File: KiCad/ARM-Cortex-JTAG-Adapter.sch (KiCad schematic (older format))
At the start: 4 parts, among them J1 Breakout I/O, J2 Power

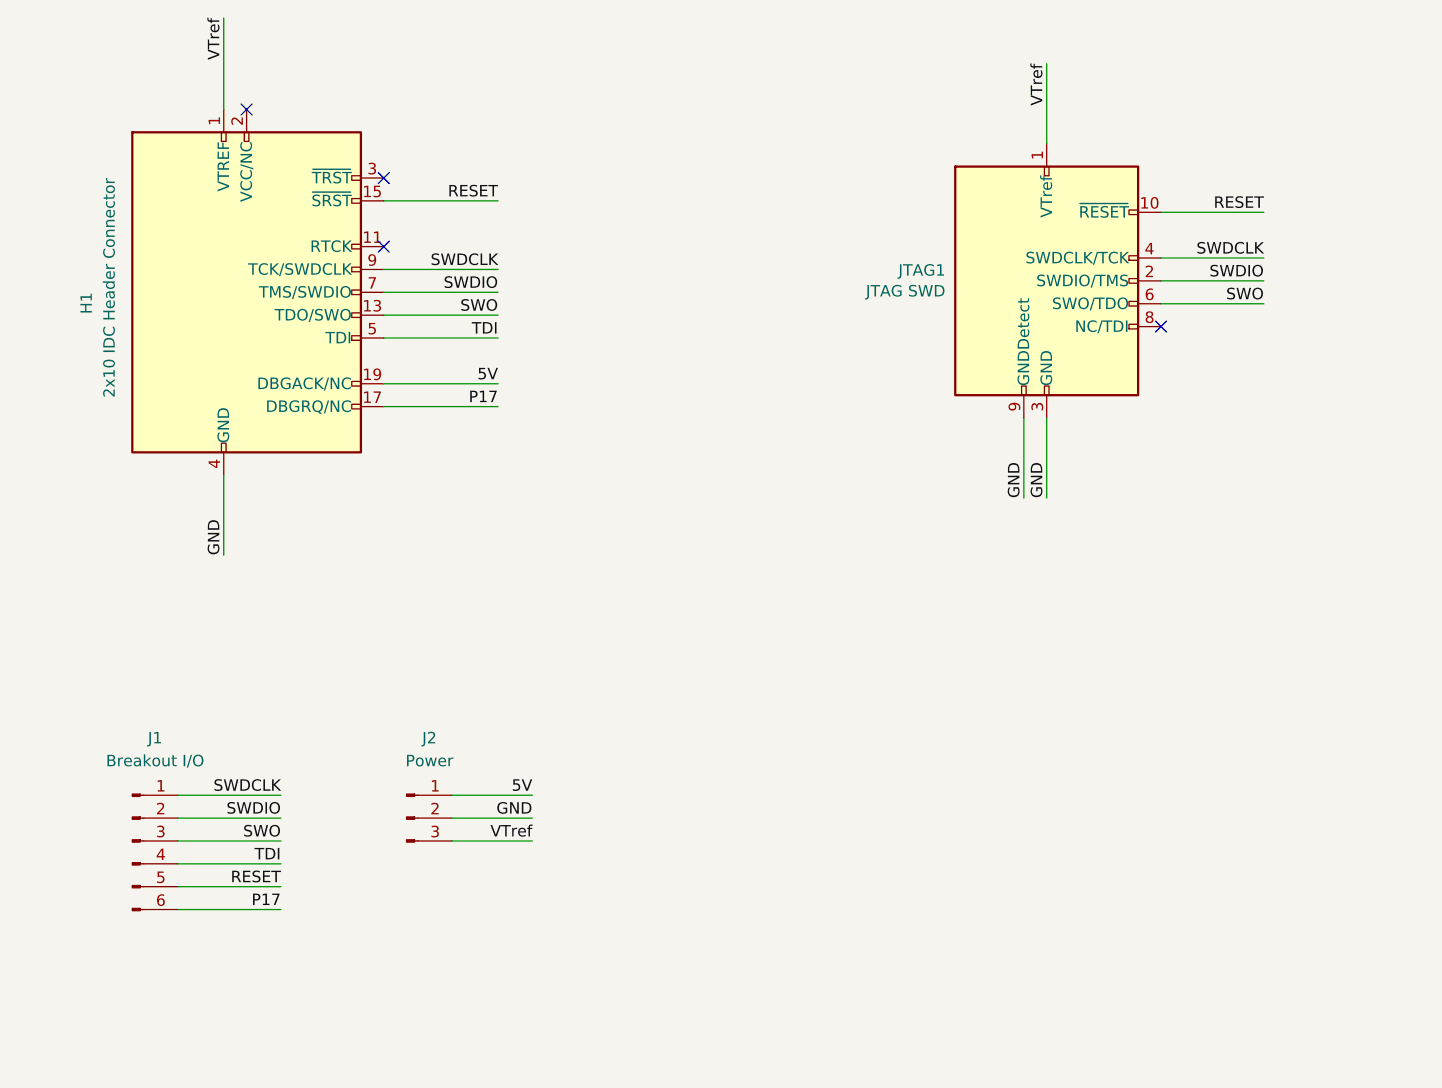
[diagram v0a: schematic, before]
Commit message: Updating schematic and PCB layout.
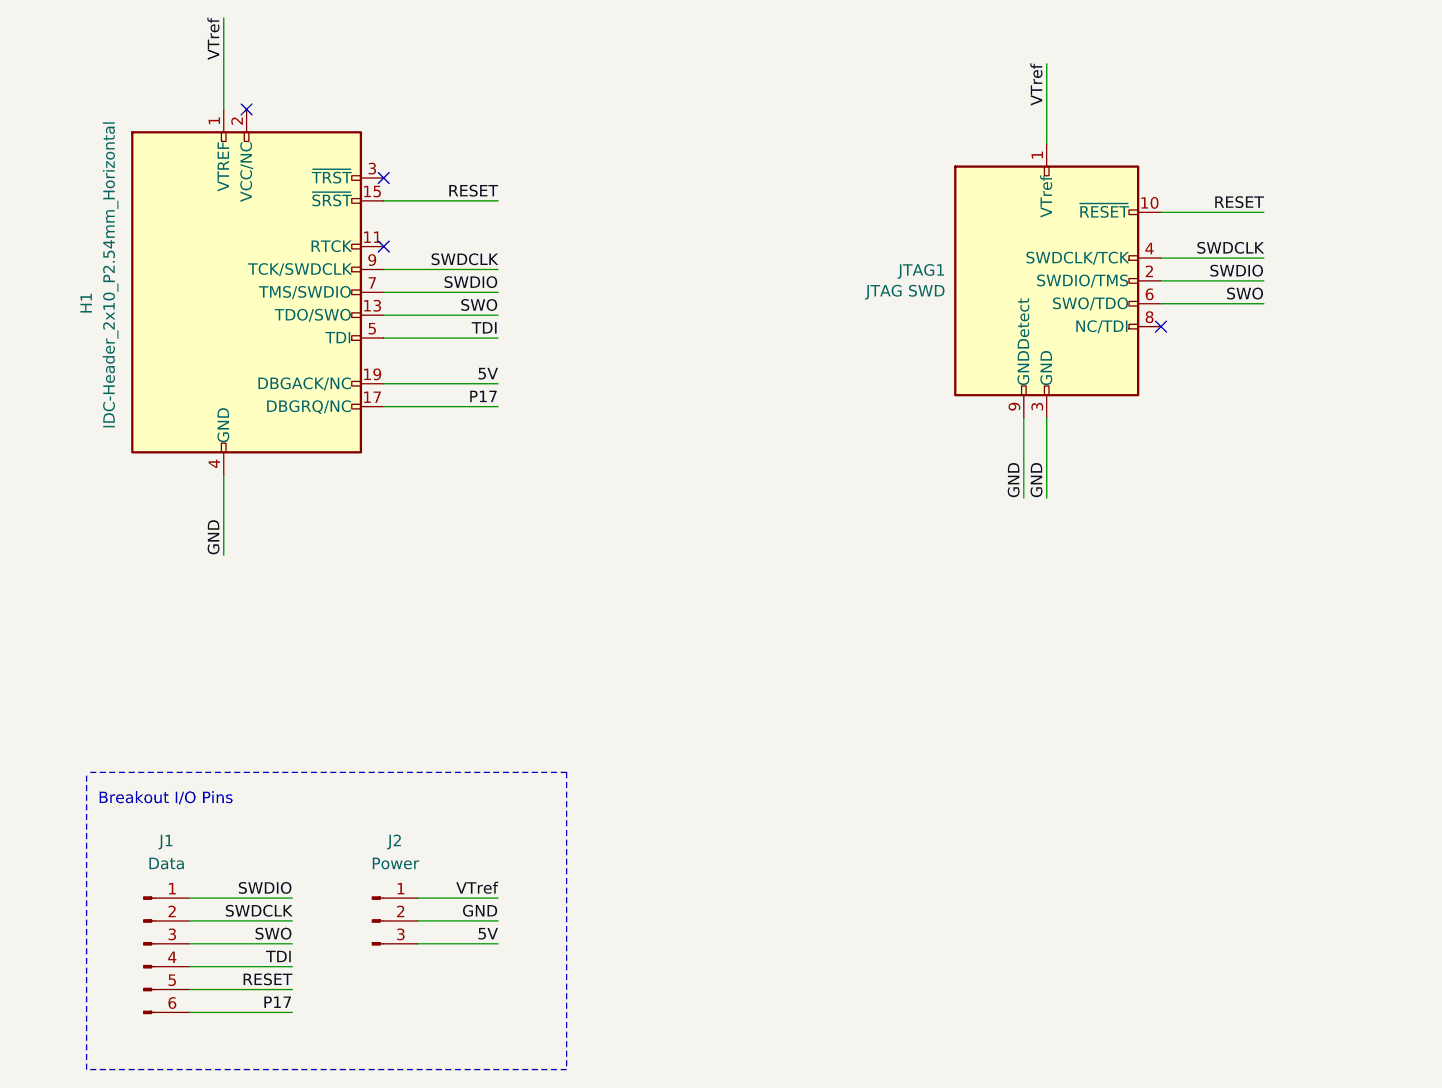
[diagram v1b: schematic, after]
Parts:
- H1: value 2x10 IDC Header Connector -> IDC-Header_2x10_P2.54mm_Horizontal
- J1: value Breakout I/O -> Data
- JTAG1: footprint Connector_PinHeader_1.27mm:PinHeader_2x05_P1.27mm_Vertical_SMD -> Connector_PinHeader_1.27mm:PinHeader_2x05_P1.27mm_Vertical
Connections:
- net 5V: now also J2.3 (Pin_3); no longer J2.1 (Pin_1)
- net SWDCLK: now also J1.2 (Pin_2); no longer J1.1 (Pin_1)
- net SWDIO: now also J1.1 (Pin_1); no longer J1.2 (Pin_2)
- net VTref: now also J2.1 (Pin_1); no longer J2.3 (Pin_3)
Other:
- note added: "Breakout I/O Pins"
- moved on the sheet: J1, J2
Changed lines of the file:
@@
 F 0 "JTAG1" H 5257 1946 50  0000 R CNN
 F 1 "JTAG SWD" H 5257 1855 50  0000 R CNN
-F 2 "Connector_PinHeader_1.27mm:PinHeader_2x05_P1.27mm_Vertical_SMD" H 5700 1900 50  0001 C CNN
+F 2 "Connector_PinHeader_1.27mm:PinHeader_2x05_P1.27mm_Vertical" H 5700 1900 50  0001 C CNN
 F 3 "http://infocenter.arm.com/help/topic/com.arm.doc.ddi0314h/DDI0314H_coresight_components_trm.pdf" V 5350 650 50  0001 C CNN
 	1    5700 1900
@@
 L Connector:Conn_01x03_Male J2
 U 1 1 5F65A72D
-P 2900 4250
-F 0 "J2" H 3000 4600 50  0000 C CNN
-F 1 "Power" H 3000 4500 50  0000 C CNN
-F 2 "Connector_PinHeader_2.54mm:PinHeader_1x03_P2.54mm_Vertical" H 2900 4250 50  0001 C CNN
-F 3 "~" H 2900 4250 50  0001 C CNN
-	1    2900 4250
+P 2750 4700
+F 0 "J2" H 2850 5050 50  0000 C CNN
+F 1 "Power" H 2850 4950 50  0000 C CNN
+F 2 "Connector_PinHeader_2.54mm:PinHeader_1x03_P2.54mm_Vertical" H 2750 4700 50  0001 C CNN
+F 3 "~" H 2750 4700 50  0001 C CNN
+	1    2750 4700
 	1    0    0    -1
 $EndComp
 Wire Wire Line
-	3100 4150 3450 4150
-Text Label 3450 4150 2    50   ~ 0
+	2950 4600 3300 4600
+Text Label 3300 4800 2    50   ~ 0
 5V
 Wire Wire Line
-	3100 4250 3450 4250
-Text Label 3450 4250 2    50   ~ 0
+	2950 4700 3300 4700
+Text Label 3300 4700 2    50   ~ 0
 GND
 Wire Wire Line
-	3100 4350 3450 4350
-Text Label 3450 4350 2    50   ~ 0
+	2950 4800 3300 4800
+Text Label 3300 4600 2    50   ~ 0
 VTref
 Wire Wire Line
-	1900 4150 2350 4150
-Text Label 2350 4150 2    50   ~ 0
+	1950 4600 2400 4600
+Text Label 2400 4700 2    50   ~ 0
 SWDCLK
 Wire Wire Line
-	1900 4250 2350 4250
-Text Label 2350 4250 2    50   ~ 0
+	1950 4700 2400 4700
+Text Label 2400 4600 2    50   ~ 0
 SWDIO
 Wire Wire Line
-	1900 4350 2350 4350
-Text Label 2350 4350 2    50   ~ 0
+	1950 4800 2400 4800
+Text Label 2400 4800 2    50   ~ 0
 SWO
 Wire Wire Line
-	1900 4450 2350 4450
-Text Label 2350 4450 2    50   ~ 0
+	1950 4900 2400 4900
+Text Label 2400 4900 2    50   ~ 0
 TDI
 $Comp
@@
 P 2200 1950
 F 0 "H1" V 1500 1950 50  0000 R CNN
-F 1 "2x10 IDC Header Connector" V 1600 2450 50  0000 R CNN
+F 1 "IDC-Header_2x10_P2.54mm_Horizontal" V 1600 2700 50  0000 R CNN
 F 2 "Connector_IDC:IDC-Header_2x10_P2.54mm_Horizontal" H 2650 900 50  0001 L TNN
 F 3 "http://infocenter.arm.com/help/topic/com.arm.doc.dui0499b/DUI0499B_system_design_reference.pdf" V 1850 700 50  0001 C CNN
@@
 P17
 Wire Wire Line
-	1900 4550 2350 4550
-Text Label 2350 4550 2    50   ~ 0
+	1950 5000 2400 5000
+Text Label 2400 5000 2    50   ~ 0
 RESET
 Wire Wire Line
-	1900 4650 2350 4650
-Text Label 2350 4650 2    50   ~ 0
+	1950 5100 2400 5100
+Text Label 2400 5100 2    50   ~ 0
 P17
 $Comp
 L Connector:Conn_01x06_Male J1
 U 1 1 5F67F15F
-P 1700 4350
-F 0 "J1" H 1800 4800 50  0000 C CNN
-F 1 "Breakout I/O" H 1800 4700 50  0000 C CNN
-F 2 "Connector_PinHeader_2.54mm:PinHeader_1x06_P2.54mm_Vertical" H 1700 4350 50  0001 C CNN
-F 3 "~" H 1700 4350 50  0001 C CNN
-	1    1700 4350
+P 1750 4800
+F 0 "J1" H 1850 5250 50  0000 C CNN
+F 1 "Data" H 1850 5150 50  0000 C CNN
+F 2 "Connector_PinHeader_2.54mm:PinHeader_1x06_P2.54mm_Vertical" H 1750 4800 50  0001 C CNN
+F 3 "~" H 1750 4800 50  0001 C CNN
+	1    1750 4800
 	1    0    0    -1
 $EndComp
+Wire Notes Line
+	3600 4050 3600 5350
+Wire Notes Line
+	3600 5350 1500 5350
+Wire Notes Line
+	1500 5350 1500 4050
+Wire Notes Line
+	3600 4050 1500 4050
+Text Notes 1550 4200 0    50   ~ 0
+Breakout I/O Pins
 $EndSCHEMATC
